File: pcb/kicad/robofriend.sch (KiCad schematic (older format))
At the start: 129 parts, among them J1 I2C, J10 BAT2, J11 5VIN, J12 BAT3, J13 3V3OUT, J14 3V3OUT, J15 SPI, J16 MON/AMP, J17 M1, J18 M2, J19 US4, J2 ADC1, J20 5VOUT, J21 5VOUT, J22 US3, J23 US2, J24 US1, J25 I2C, J26 I2C, J27 I2C, J28 ADC4, J3 ADC2, J30 PWR, J31 MLe, J32 USB_A_4_PIN, J4 UART, J5 ADC3, J6 ADC4, J7 BAT1, J8 MRi, J9 12VOUT, K2 SCHRACK-RTx3, Q1 NMOS, Q2 NMOS, Q3 NPN, Q4 PMOS, Q5 NMOS, Q6 NMOS, Q7 NMOS, Q8 NMOS, Q9 NPN, U1 Teensy++2.0, U2 LM4040, U3 LM358, U5 LM3940-3.3

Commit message: new vbat measurement logic, adding an impedance converter
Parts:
- removed C12: 100n, Capacitors_SMD:C_0805, symbol C
- removed D12: 5V1, Diodes_SMD:D_SOD-123, symbol D_Zener
- added D? (x2): D_Schottky, symbol D_Schottky
- added U?: INA193, TO_SOT_Packages_SMD:SOT-23-5, symbol INA193
- added U?: LM321, TO_SOT_Packages_SMD:SOT-23-5, symbol LM321
- R10: value 100k -> 8.2k
- R11: value 27k -> 2.2k
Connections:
- net +5V: now also D?.1 (K), U?.5 (V+)
- net F0: now also U?.3 (-), U?.4; no longer R10.1, R11.1
- net GND: now also D?.2 (A), U?.2 (V-)
- new net: D?.1 (K), D?.2 (A), R10.1, R11.1, U?.1 (+)
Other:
- moved on the sheet: R10, R11
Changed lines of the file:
@@
 L R R10
 U 1 1 5B2CB2AA
-P 13900 3450
-F 0 "R10" V 13980 3450 50  0000 C CNN
-F 1 "100k" V 13900 3450 50  0000 C CNN
-F 2 "Resistors_SMD:R_0805" V 13830 3450 50  0001 C CNN
-F 3 "" H 13900 3450 50  0001 C CNN
-	1    13900 3450
+P 17150 3950
+F 0 "R10" V 17230 3950 50  0000 C CNN
+F 1 "8.2k" V 17150 3950 50  0000 C CNN
+F 2 "Resistors_SMD:R_0805" V 17080 3950 50  0001 C CNN
+F 3 "" H 17150 3950 50  0001 C CNN
+	1    17150 3950
 	0    1    1    0
 $EndComp
@@
 L R R11
 U 1 1 5B2CB7A9
-P 14150 3800
-F 0 "R11" V 14230 3800 50  0000 C CNN
-F 1 "27k" V 14150 3800 50  0000 C CNN
-F 2 "Resistors_SMD:R_0805" V 14080 3800 50  0001 C CNN
-F 3 "" H 14150 3800 50  0001 C CNN
-	1    14150 3800
+P 17400 4200
+F 0 "R11" V 17480 4200 50  0000 C CNN
+F 1 "2.2k" V 17400 4200 50  0000 C CNN
+F 2 "Resistors_SMD:R_0805" V 17330 4200 50  0001 C CNN
+F 3 "" H 17400 4200 50  0001 C CNN
+	1    17400 4200
 	1    0    0    -1
 $EndComp
 $Comp
-L C C12
-U 1 1 5B2CBA4F
-P 14650 3800
-F 0 "C12" H 14540 3710 50  0000 L CNN
-F 1 "100n" H 14445 3890 50  0000 L CNN
-F 2 "Capacitors_SMD:C_0805" H 14688 3650 50  0001 C CNN
-F 3 "" H 14650 3800 50  0001 C CNN
-	1    14650 3800
-	-1   0    0    1
-$EndComp
-$Comp
-L D_Zener D12
-U 1 1 5B2CBB74
-P 15150 3800
-F 0 "D12" V 15050 3875 50  0000 C CNN
-F 1 "5V1" V 15250 3900 50  0000 C CNN
-F 2 "Diodes_SMD:D_SOD-123" H 15150 3800 50  0001 C CNN
-F 3 "" H 15150 3800 50  0001 C CNN
-	1    15150 3800
-	0    1    1    0
-$EndComp
-$Comp
 L Q_PMOS_DGS Q4
 U 1 1 5B2D2545
@@
 L GND #PWR034
 U 1 1 5B2FB285
-P 13650 4250
-F 0 "#PWR034" H 13650 4000 50  0001 C CNN
-F 1 "GND" H 13650 4100 50  0000 C CNN
-F 2 "" H 13650 4250 50  0001 C CNN
-F 3 "" H 13650 4250 50  0001 C CNN
-	1    13650 4250
+P 17900 4550
+F 0 "#PWR034" H 17900 4300 50  0001 C CNN
+F 1 "GND" H 17900 4400 50  0000 C CNN
+F 2 "" H 17900 4550 50  0001 C CNN
+F 3 "" H 17900 4550 50  0001 C CNN
+	1    17900 4550
 	1    0    0    -1
 $EndComp
@@
 Text GLabel 4900 8200 0    60   Input ~ 0
 D1
-Text GLabel 15350 3450 2    60   Input ~ 0
+Text GLabel 19300 3850 2    60   Input ~ 0
 F0
 $Comp
@@
 	1    0    0    -1
 $EndComp
-Text Notes 14775 2925 2    79   ~ 0
+Text Notes 18075 2975 2    79   ~ 0
 VBat Measurement
 Text Notes 11400 875  2    79   ~ 0
@@
 L +12V #PWR078
 U 1 1 5B3E4B8A
-P 13650 3350
-F 0 "#PWR078" H 13650 3200 50  0001 C CNN
-F 1 "+12V" H 13650 3490 50  0000 C CNN
-F 2 "" H 13650 3350 50  0001 C CNN
-F 3 "" H 13650 3350 50  0001 C CNN
-	1    13650 3350
+P 16900 3850
+F 0 "#PWR078" H 16900 3700 50  0001 C CNN
+F 1 "+12V" H 16900 3990 50  0000 C CNN
+F 2 "" H 16900 3850 50  0001 C CNN
+F 3 "" H 16900 3850 50  0001 C CNN
+	1    16900 3850
 	1    0    0    -1
 $EndComp
@@
 	0    -1   -1   0
 $EndComp
+$Comp
+L +5V #PWR?
+U 1 1 5B4640E6
+P 7650 4200
+F 0 "#PWR?" H 7650 4050 50  0001 C CNN
+F 1 "+5V" H 7650 4340 50  0000 C CNN
+F 2 "" H 7650 4200 50  0001 C CNN
+F 3 "" H 7650 4200 50  0001 C CNN
+	1    7650 4200
+	-1   0    0    -1
+$EndComp
+$Comp
+L INA193 U?
+U 1 1 5B466E12
+P 6050 4200
+F 0 "U?" H 6200 4350 50  0000 C CNN
+F 1 "INA193" H 6200 4050 50  0000 C CNN
+F 2 "TO_SOT_Packages_SMD:SOT-23-5" H 6050 4200 50  0001 C CNN
+F 3 "" H 6050 4200 50  0001 C CNN
+	1    6050 4200
+	1    0    0    -1
+$EndComp
+$Comp
+L D_Schottky D?
+U 1 1 5B46DF42
+P 17900 3600
+F 0 "D?" H 17900 3700 50  0000 C CNN
+F 1 "D_Schottky" H 17900 3500 50  0000 C CNN
+F 2 "" H 17900 3600 50  0001 C CNN
+F 3 "" H 17900 3600 50  0001 C CNN
+	1    17900 3600
+	0    1    1    0
+$EndComp
+$Comp
+L D_Schottky D?
+U 1 1 5B46E631
+P 17900 4200
+F 0 "D?" H 17900 4300 50  0000 C CNN
+F 1 "D_Schottky" H 17900 4100 50  0000 C CNN
+F 2 "" H 17900 4200 50  0001 C CNN
+F 3 "" H 17900 4200 50  0001 C CNN
+	1    17900 4200
+	0    1    1    0
+$EndComp
+$Comp
+L +5V #PWR?
+U 1 1 5B46F020
+P 17900 3400
+F 0 "#PWR?" H 17900 3250 50  0001 C CNN
+F 1 "+5V" H 17900 3540 50  0000 C CNN
+F 2 "" H 17900 3400 50  0001 C CNN
+F 3 "" H 17900 3400 50  0001 C CNN
+	1    17900 3400
+	1    0    0    -1
+$EndComp
+$Comp
+L LM321 U?
+U 1 1 5B46F1B8
+P 18700 3850
+F 0 "U?" H 18700 4150 50  0000 L CNN
+F 1 "LM321" H 18700 4050 50  0000 L CNN
+F 2 "TO_SOT_Packages_SMD:SOT-23-5" H 18700 3850 50  0001 C CNN
+F 3 "" H 18700 3850 50  0001 C CNN
+	1    18700 3850
+	1    0    0    -1
+$EndComp
+$Comp
+L +5V #PWR?
+U 1 1 5B47136A
+P 18600 3400
+F 0 "#PWR?" H 18600 3250 50  0001 C CNN
+F 1 "+5V" H 18600 3540 50  0000 C CNN
+F 2 "" H 18600 3400 50  0001 C CNN
+F 3 "" H 18600 3400 50  0001 C CNN
+	1    18600 3400
+	1    0    0    -1
+$EndComp
+$Comp
+L GND #PWR?
+U 1 1 5B471501
+P 18600 4250
+F 0 "#PWR?" H 18600 4000 50  0001 C CNN
+F 1 "GND" H 18600 4100 50  0000 C CNN
+F 2 "" H 18600 4250 50  0001 C CNN
+F 3 "" H 18600 4250 50  0001 C CNN
+	1    18600 4250
+	1    0    0    -1
+$EndComp
 Wire Wire Line
 	1600 10100 2050 10100
@@
 Connection ~ 3350 6100
 Wire Wire Line
-	3350 5750 3350 6000
+	3350 6100 3350 6000
 Wire Wire Line
-	3350 6000 3350 6100
+	3350 6000 3350 5750
 Wire Notes Line
 	13250 7650 13250 8000
@@
 	6650 1550 6750 1550
 Wire Wire Line
-	13650 3450 13650 3350
+	16900 3950 16900 3850
 Wire Wire Line
 	3350 6000 3250 6000
@@
 Wire Wire Line
 	2100 2150 1600 2150
-Connection ~ 14150 4150
-Wire Wire Line
-	13650 4150 13650 4250
-Wire Wire Line
-	15150 4150 15150 3950
 Wire Wire Line
 	3250 2550 3300 2550
@@
 	5450 2250 5350 2250
 Wire Wire Line
-	14050 3450 14150 3450
-Wire Wire Line
-	14150 3450 14650 3450
-Wire Wire Line
-	14650 3450 15150 3450
-Wire Wire Line
-	15150 3450 15350 3450
-Wire Wire Line
-	13750 3450 13650 3450
+	17000 3950 16900 3950
 Wire Wire Line
 	4300 5500 4300 5150
@@
 Wire Wire Line
 	1600 5100 1650 5100
-Connection ~ 14650 4150
-Wire Wire Line
-	14150 4150 14150 3950
-Wire Wire Line
-	14650 4150 14650 3950
 Wire Wire Line
-	13650 4150 14150 4150
+	17400 4350 17400 4450
 Wire Wire Line
-	14150 4150 14650 4150
+	17900 4350 17900 4450
 Wire Wire Line
-	14650 4150 15150 4150
-Connection ~ 15150 3450
-Connection ~ 14650 3450
+	17900 4450 17900 4550
 Wire Wire Line
-	15150 3450 15150 3650
-Connection ~ 14150 3450
+	17900 3750 17900 3950
 Wire Wire Line
-	14650 3450 14650 3650
+	17900 3950 17900 4050
 Wire Wire Line
-	14150 3450 14150 3650
+	17400 3950 17400 4050
 Connection ~ 9050 10000
 Wire Wire Line
@@
 Connection ~ 13650 8400
 Wire Notes Line
-	13400 2700 15050 2700
+	16700 2750 18350 2750
 Wire Notes Line
-	13400 3050 15650 3050
+	16700 3100 19600 3100
 Wire Notes Line
-	13400 4600 13400 2700
+	16700 4850 16700 2750
 Wire Notes Line
-	15050 2700 15050 3050
+	18350 2750 18350 3100
 Wire Notes Line
-	15650 3050 15650 4600
+	19600 3100 19600 4850
 Wire Notes Line
-	15650 4600 13400 4600
+	19600 4850 16700 4850
 Wire Notes Line
 	9900 650  11550 650
@@
 	5800 4700 5800 4850
 Wire Wire Line
-	7050 6100 5800 6100
+	1950 6100 2450 6100
 Wire Wire Line
-	5800 6100 5300 6100
+	2450 6100 3350 6100
 Wire Wire Line
-	5300 6100 4800 6100
+	3350 6100 3850 6100
 Wire Wire Line
-	4800 6100 4300 6100
+	3850 6100 4300 6100
 Wire Wire Line
-	4300 6100 3850 6100
+	4300 6100 4800 6100
 Wire Wire Line
-	3850 6100 3350 6100
+	4800 6100 5300 6100
 Wire Wire Line
-	3350 6100 2450 6100
+	5300 6100 5800 6100
 Wire Wire Line
-	2450 6100 1950 6100
+	5800 6100 7050 6100
 Wire Wire Line
 	4800 5850 4800 6100
@@
 Connection ~ 7050 5550
 Wire Wire Line
-	7050 5350 7050 5550
+	7050 6100 7050 5550
 Wire Wire Line
-	7050 5550 7050 6100
+	7050 5550 7050 5350
 Wire Wire Line
 	6700 5550 7050 5550
@@
 	7650 4300 7650 4200
 Connection ~ 5800 6100
-$Comp
-L +5V #PWR?
-U 1 1 5B4640E6
-P 7650 4200
-F 0 "#PWR?" H 7650 4050 50  0001 C CNN
-F 1 "+5V" H 7650 4340 50  0000 C CNN
-F 2 "" H 7650 4200 50  0001 C CNN
-F 3 "" H 7650 4200 50  0001 C CNN
-	1    7650 4200
-	-1   0    0    -1
-$EndComp
+Wire Wire Line
+	17900 3450 17900 3400
+Wire Wire Line
+	17300 3950 17400 3950
+Wire Wire Line
+	17400 3950 17900 3950
+Wire Wire Line
+	17900 3950 18400 3950
+Connection ~ 17900 3950
+Connection ~ 17400 3950
+Wire Wire Line
+	18400 3750 18200 3750
+Wire Wire Line
+	18200 3750 18200 3500
+Wire Wire Line
+	18200 3500 19200 3500
+Wire Wire Line
+	19200 3500 19200 3850
+Wire Wire Line
+	19000 3850 19200 3850
+Wire Wire Line
+	19200 3850 19300 3850
+Wire Wire Line
+	18600 3550 18600 3400
+Wire Wire Line
+	18600 4150 18600 4250
+Connection ~ 19200 3850
+Connection ~ 17900 4450
+Wire Wire Line
+	17400 4450 17900 4450
 $EndSCHEMATC

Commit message: added a jumper for the external aref voltage since the internal vref may not be used if an external vref is being applied to the AREF pin
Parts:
- added JP?: JP, Pin_Headers:Pin_Header_Straight_1x02_Pitch2.54mm, symbol Jumper_NO_Small
- R8: value 909 -> 910
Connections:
- net AREF: now also JP?.1; no longer R8.2, U2.1 (Cathode)
- new net: JP?.2, R8.2, U2.1 (Cathode)
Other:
- note added: "R = (5V - 4.096V) / 1mA\nR = 904 Ohm\nR = (5V -3V) / 1mA\nR = 2k Ohm"
- note removed: "R = (5V - 4.096V) / 1mA\nR = 904 Ohm"
- moved on the sheet: R8, U2

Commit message: completed the new overcurrent protection circuit using INA193, added a free-wheeling diode for the consumer
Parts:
- removed D22: LED, LEDs:LED_0805, symbol LED
- removed Q9: NPN, TO_SOT_Packages_SMD:SOT-23, symbol Q_NPN_BCE
- removed R19, R20: 33k, Resistors_SMD:R_0805, symbol R
- removed R28: 1k, Resistors_SMD:R_0805, symbol R
- removed R29: 10k, Resistors_SMD:R_0805, symbol R
- removed R30: 330, Resistors_SMD:R_0805, symbol R
- removed U3: LM358, SMD_Packages:SOIC-8-N, symbol LM358
- added C12: 1n, symbol C
- added C25, C26: 100n, Capacitors_SMD:C_0805, symbol C
- added D22: BAT54, symbol D_Schottky
- added U4: OPA344, symbol OPA340NA
- C23: value 100n -> 10n; footprint Capacitors_SMD:C_0805 -> (none)
- C24: value 100n -> 1n; footprint Capacitors_SMD:C_0805 -> (none)
- D12, D23: renamed from D?; value D_Schottky -> BAT54
- R17, R18: value 1k -> 100
- gave numbers to parts that had none: 3
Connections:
- net +12V: no longer C23.2, C24.2
- net +5V: now also U3.5 (V+), C25.2, C26.2, U4.5 (V+)
- net E6: now also U4.1
- net GND: now also C24.2, U3.2 (GND), C12.1, C25.1, C26.1, D22.2 (A), U4.2 (V-); no longer C23.1, C24.1
- net at R17.1: now also C23.1, U3.3 (+), C12.2
- net at R18.1: now also C23.2, C24.1, U3.4 (-)
- net at J17.1 (Pin_1), J18.1 (Pin_1), R15.2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: now also D22.1 (K)
- net at RV2.2: now also U4.4 (-)
- net at U3.1: now also U4.3 (+)
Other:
- note removed: "OC_INT"
- moved on the sheet: R17, R18, RV2, U3

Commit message: minor corrections and beautification before implementing the battery charge logic
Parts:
- C12, C23, C24: footprint (none) -> Capacitors_SMD:C_0603
- D12, D22, D23: footprint (none) -> Diodes_SMD:D_SOD-123
- U4: footprint (none) -> TO_SOT_Packages_SMD:SOT-23-5
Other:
- note added: "R = (5V - 4.096V) / 1mA = 904 Ohm\nR = (5V -3V) / 1mA = 2k Ohm"
- note removed: "R = (5V - 4.096V) / 1mA\nR = 904 Ohm\nR = (5V -3V) / 1mA\nR = 2k Ohm"
- moved on the sheet: C1, C10, C11, C12, C13, C14, C15, C16, C17, C18, C19, C2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

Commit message: added new spice simulation for battery discharge and overcharge protection circuit
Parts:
- C12, C23, C24: footprint Capacitors_SMD:C_0603 -> Capacitors_SMD:C_0805

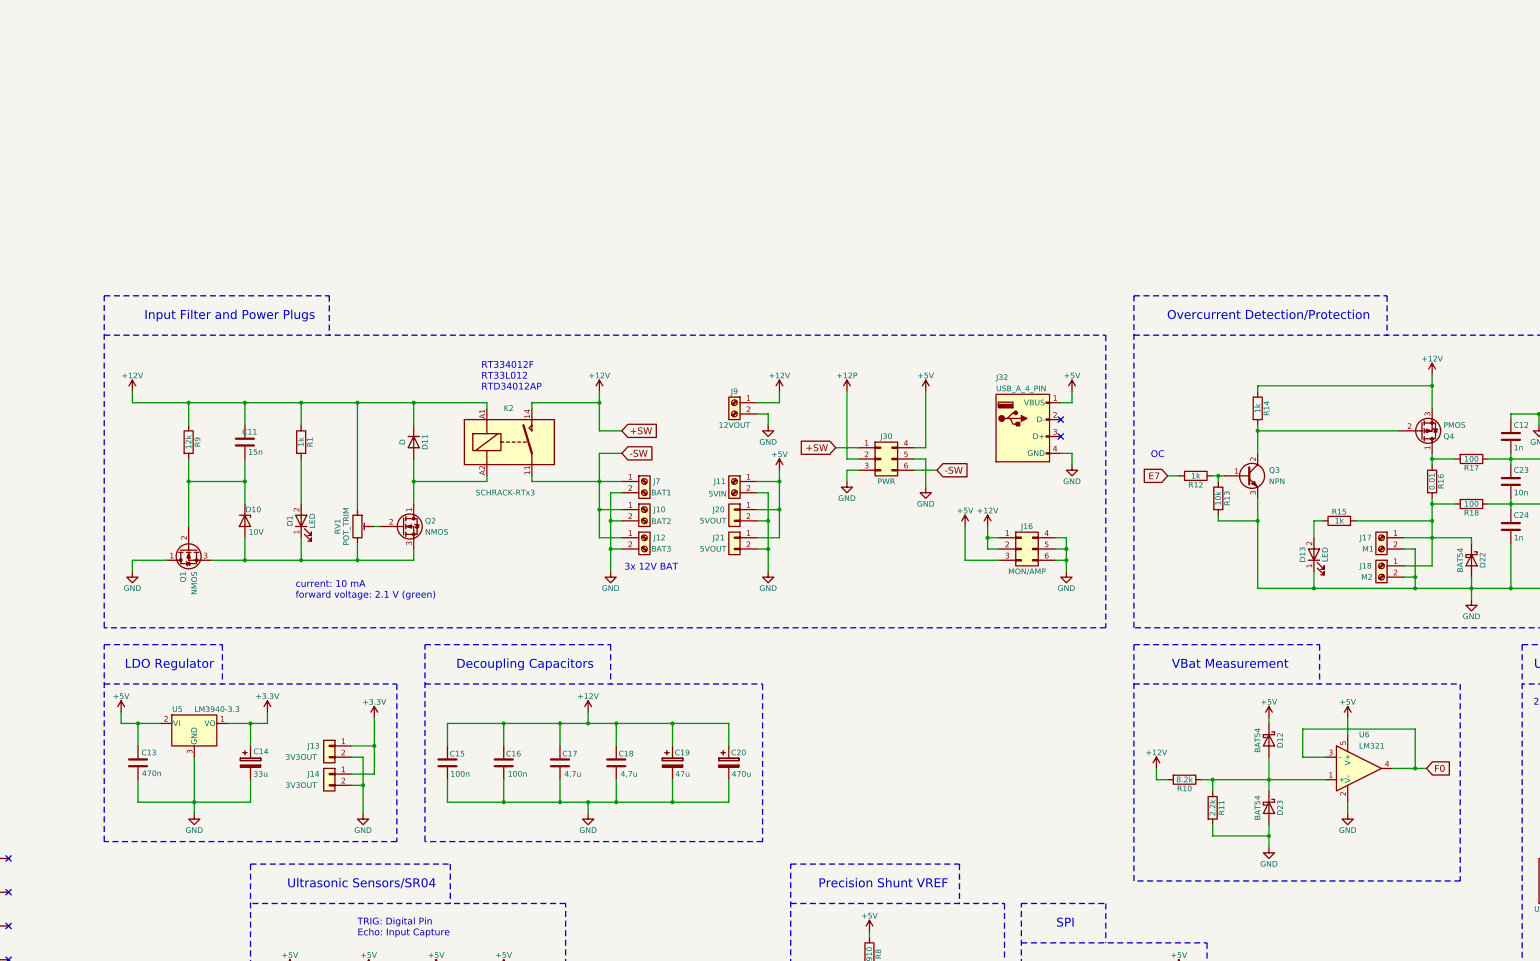
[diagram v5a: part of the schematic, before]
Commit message: kicad circuit adopted to the new simulation circuit
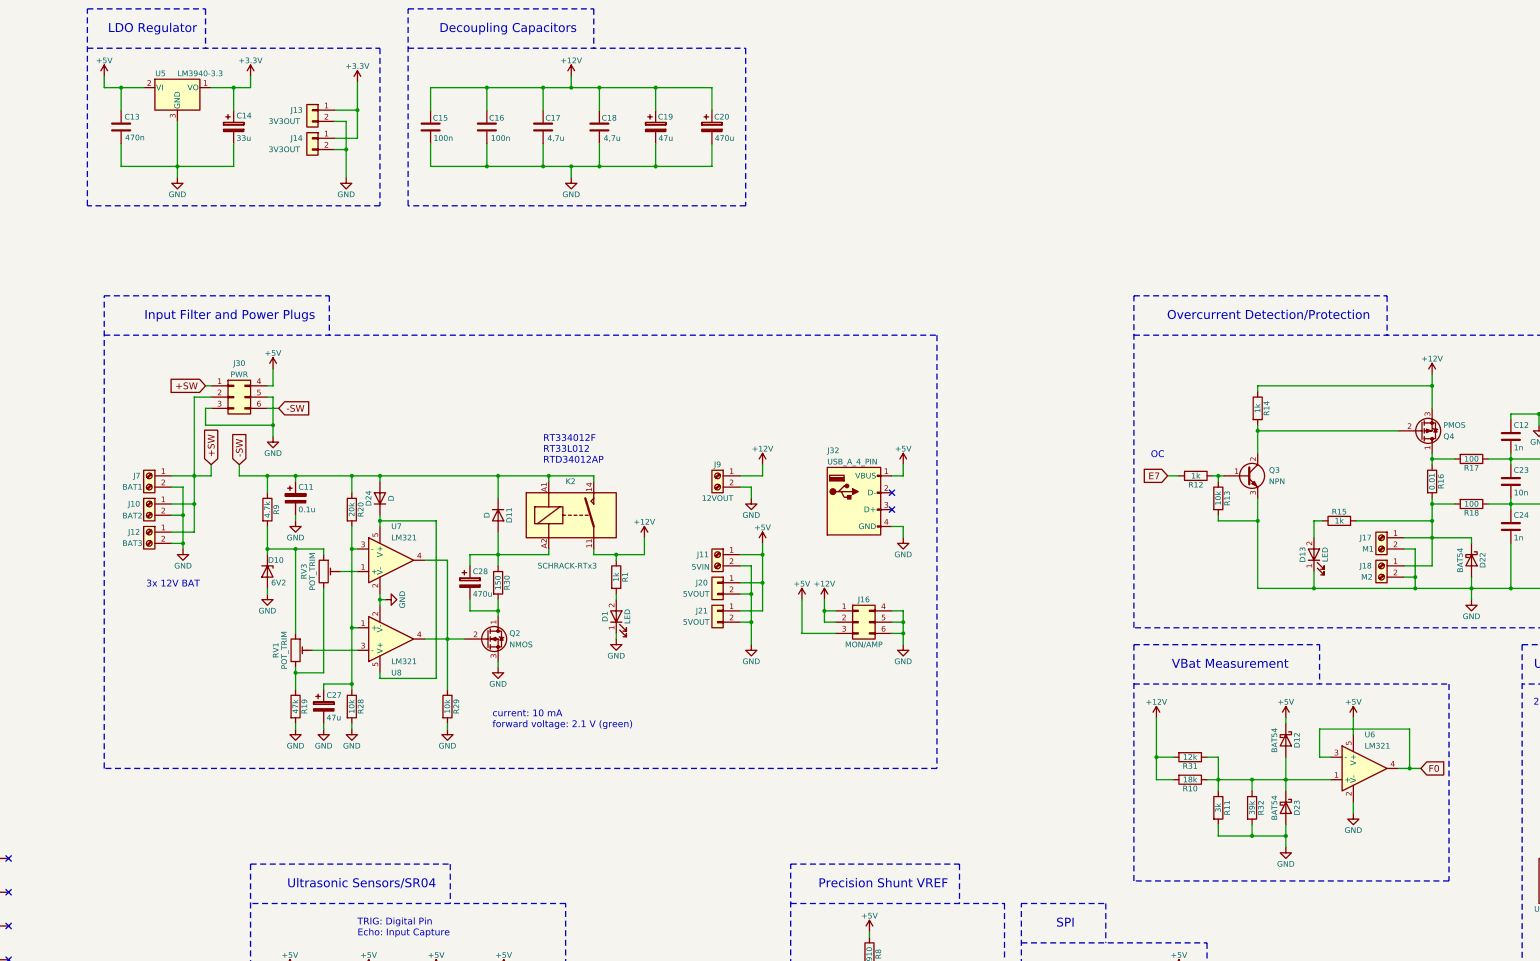
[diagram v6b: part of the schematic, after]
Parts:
- removed C11: 15n, Capacitors_SMD:C_0805, symbol C
- removed Q1: NMOS, TO_SOT_Packages_THT:TO-220-3_Vertical, symbol Q_NMOS_DGS
- added C11: 0.1u, symbol CP
- added C27: 47u, symbol CP
- added C28: 470u, symbol CP
- added D24: D, Diodes_SMD:D_SOD-523, symbol D
- added R19: 47k, Resistors_SMD:R_0805, symbol R
- added R20: 20k, Resistors_SMD:R_0805, symbol R
- added R28, R29: 10k, Resistors_SMD:R_0805, symbol R
- added R30: 150, Resistors_SMD:R_0805, symbol R
- added R31: 12k, Resistors_SMD:R_0805, symbol R
- added R32: 39k, Resistors_SMD:R_0805, symbol R
- added RV3: POT_TRIM, Potentiometers:Potentiometer_Trimmer_Bourns_3296W, symbol POT_TRIM
- added U7, U8: LM321, TO_SOT_Packages_SMD:SOT-23-5, symbol LM321
- D10: value 10V -> 6V2
- R10: value 8.2k -> 18k
- R11: value 2.2k -> 3k
- R9: value 12k -> 4.7k
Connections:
- net +12V: now also K2.11, R31.2; no longer D11.1 (K), J30.1 (Pin_1), K2.14, K2.A1, R9.1, RV1.1
- net -SW: now also D11.1 (K), K2.14, K2.A1, R9.1, C11.1, D24.2 (A), R20.1; no longer J10.1 (Pin_1), J12.1 (Pin_1), J7.1 (Pin_1), K2.11
- net GND: now also D1.1 (K), D10.2 (A), Q2.3 (S), C11.2, C27.2, R19.2, R28.2, R29.2, R32.2, U7.2 (V-), U8.2 (V-)
- net at D10.1 (K), R9.2: now also RV1.1, RV3.1
- net at Q2.2 (G): now also R29.1, U7.4, U8.4; no longer RV1.2
- net at D11.2 (A), K2.A2: now also C28.1, R30.1; no longer Q2.1 (D)
- net at D12.2 (A), D23.1 (K), R10.1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: now also R31.1, R32.1
- net +12P renamed +SW
- net +SW: now also J10.1 (Pin_1), J12.1 (Pin_1), J30.1 (Pin_1), J7.1 (Pin_1)
- new net: C28.2, Q2.1 (D), R30.2
- new net: C27.1, R20.2, R28.1, U7.3 (-), U8.1 (+)
- new net: RV3.2, U7.1 (+)
- new net: R19.1, RV1.3, RV3.3
- new net: RV1.2, U8.3 (-)
- new net: D24.1 (K), U7.5 (V+), U8.5 (V+)
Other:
- moved on the sheet: C13, C14, C15, C16, C17, C18, C19, C20, D1, D10, D11, D12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

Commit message: completed first major version, waiting for feedback to start with the layout
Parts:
- removed C28: 470u, symbol CP
- removed R29: 10k, Resistors_SMD:R_0805, symbol R
- removed R30: 150, Resistors_SMD:R_0805, symbol R
- removed RV3: POT_TRIM, Potentiometers:Potentiometer_Trimmer_Bourns_3296W, symbol POT_TRIM
- removed U4: OPA344, TO_SOT_Packages_SMD:SOT-23-5, symbol OPA340NA
- removed U6, U7, U8: LM321, TO_SOT_Packages_SMD:SOT-23-5, symbol LM321
- added J33, J?: GS2, Connectors:GS2, symbol GS2
- added R?: 1M, Resistors_SMD:R_0805, symbol R
- added U4: MCP6001, TO_SOT_Packages_SMD:SOT-23-5, symbol MCP6001
- added U6: TL331, TO_SOT_Packages_SMD:SOT-23-5, symbol TL331
- added U?: TL331, symbol TL331
- C27: value 47u -> 33u
- K2: footprint SLA_12VDC:Relay_SPST_Schrack-RTx3_RM3.5mm -> Relay:SPST_Schrack-RTx3_RM3.5mm
- Q2: footprint TO_SOT_Packages_THT:TO-220-3_Vertical -> TO_SOT_Packages_SMD:SOT-23
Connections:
- net +5V: now also U4.5 (V+), U6.5 (V+)
- net E6: now also U6.4
- net F0: now also U4.1, U4.4 (-)
- net F6: now also J33.1 (G1)
- net GND: now also U4.2 (V-), U6.2 (V-), U?.2 (V-)
- net at Q2.1 (D): now also D11.2 (A), K2.A2
- net at Q2.2 (G): now also R?.1, U?.4
- net at D12.2 (A), D23.1 (K), R10.1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: now also U4.3 (+)
- net at RV2.2: now also U6.1 (-)
- net at U3.1: now also J33.2 (G2), U6.3 (+)
- net at R20.2, R28.1: now also J?.2 (G2), R?.2, U?.3 (+); no longer C27.1
- net at RV1.2: now also U?.1 (-)
- net at D24.1 (K): now also U?.5 (V+)
- new net: C27.1, J?.1 (G1)
- no-connect marks 33 -> 32
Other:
- note added: "OC_INT"
- moved on the sheet: C11, C13, C14, C15, C16, C17, C18, C19, C20, C26, C27, D1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

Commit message: completed CvPcb to assosiate components and footprints
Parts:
- gave numbers to parts that had none: 3
- renumbered C13 to C1, C18 to C10, C19 to C11, C20 to C12, C21 to C13, C22 to C14, C3 to C15, C4 to C16, C12 to C17, C23 to C18, C24 to C19, C1 to C2, C5 to C20, C25 to C21, C6 to C22, C9 to C23, C26 to C24, C10 to C25, C7 to C26, C8 to C27, C2 to C3, C14 to C4, C11 to C5, C27 to C6, C15 to C7, C16 to C8, C17 to C9, D10 to D1, D19 to D10, D8 to D11, D9 to D12, D20 to D13, D21 to D14, D12 to D15, D23 to D16, D13 to D17, D2 to D18, D3 to D19, D24 to D2, D22 to D20, D6 to D21, D7 to D22, D4 to D23, D5 to D24, D11 to D3, D1 to D4, D14 to D5, D15 to D6, D16 to D7, D17 to D8, D18 to D9, J7 to J1, J22 to J10, J19 to J11, J1 to J12, J25 to J13, J26 to J14, J27 to J15, J9 to J16, J11 to J17, J20 to J18, J21 to J19, J10 to J2, J32 to J20, J16 to J21, J6 to J22, J8 to J23, J15 to J24, J28 to J25, J31 to J26, J17 to J27, J18 to J28, J2 to J29, J12 to J3, J3 to J30, J4 to J31, J5 to J32, J30 to J4, J24 to J5, J13 to J6, J14 to J7, J23 to J9, JP6 to JP2, JP7 to JP3, JP3 to JP4, JP4 to JP5, JP2 to JP6, JP5 to JP7, K2 to K1, Q2 to Q1, Q7 to Q2, Q8 to Q3, Q3 to Q4, Q4 to Q5, Q5 to Q6, Q6 to Q7, R9 to R1, R26 to R10, R27 to R11, R5 to R12, R31 to R13, R10 to R14, R12 to R15, R11 to R16, R13 to R17, R32 to R18, R21 to R19, R19 to R2, R14 to R20, R15 to R21, R16 to R22, R2 to R23, R17 to R24, R18 to R25, R4 to R26, R22 to R27, R23 to R28, R3 to R29, R20 to R3, R24 to R30, R25 to R31, R28 to R4, R1 to R6, R6 to R7, R7 to R8, R8 to R9, U5 to U1, U1 to U2, U2 to U4, U4 to U5, U3 to U6, U6 to U7
